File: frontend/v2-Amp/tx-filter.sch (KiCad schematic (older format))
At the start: 98 parts, among them K10 HK4100, K11 HK4100, K12 HK4100, K13 HK4100, K14 HK4100, K15 HK4100, K2 HK4100, K3 HK4100, K4 HK4100, K5 HK4100, K6 HK4100, K7 HK4100, K8 HK4100, K9 HK4100

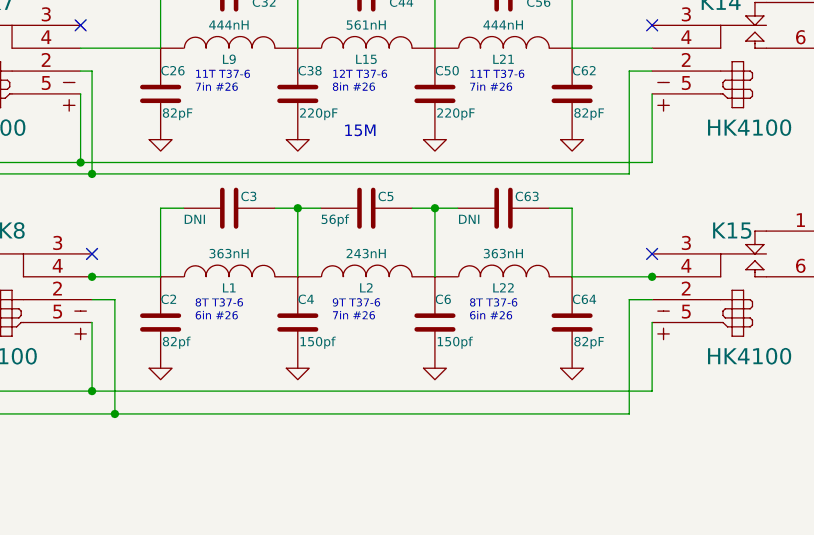
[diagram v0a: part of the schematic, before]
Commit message: Updates to 10M filter
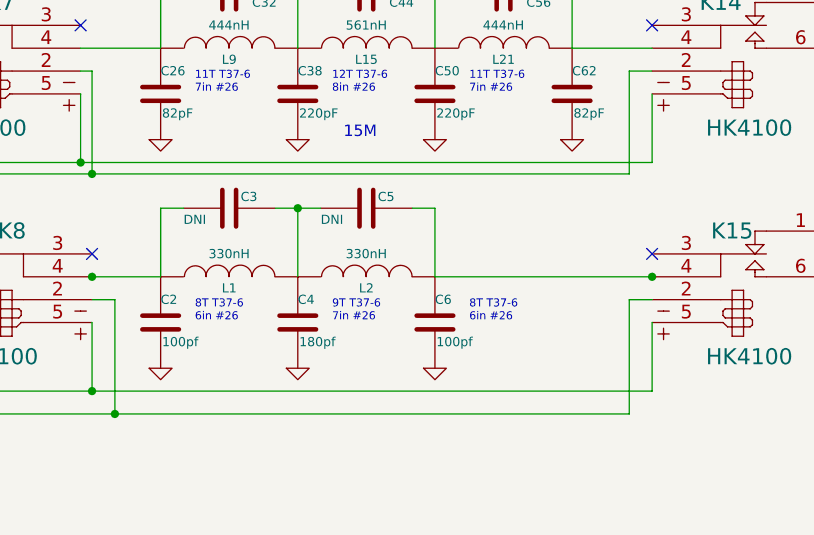
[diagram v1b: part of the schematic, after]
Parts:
- removed C63: DNI, HERMESLITE:C_0805, symbol C-RESCUE-amp
- removed C64: 82pF, HERMESLITE:C_0805, symbol C-RESCUE-amp
- removed L22: 363nH, Resistors_SMD:R_0805_HandSoldering, symbol INDUCTOR
- C2: value 82pf -> 100pf
- C4: value 150pf -> 180pf
- C5: value 56pf -> DNI
- C6: value 150pf -> 100pf
- L1: value 363nH -> 330nH; footprint Resistors_SMD:R_0805_HandSoldering -> HERMESLITE:inductor
- L2: value 243nH -> 330nH; footprint Resistors_SMD:R_0805_HandSoldering -> HERMESLITE:inductor
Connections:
- net at K15.4: now also C5.1, C6.1, L2.2
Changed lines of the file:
@@
 P 3900 6300
 F 0 "L1" V 3850 6300 40  0000 C CNN
-F 1 "363nH" V 4000 6300 40  0000 C CNN
-F 2 "Resistors_SMD:R_0805_HandSoldering" H 3900 6300 60  0001 C CNN
+F 1 "330nH" V 4000 6300 40  0000 C CNN
+F 2 "HERMESLITE:inductor" H 3900 6300 60  0001 C CNN
 F 3 "" H 3900 6300 60  0000 C CNN
 	1    3900 6300
@@
 P 4500 6300
 F 0 "L2" V 4450 6300 40  0000 C CNN
-F 1 "243nH" V 4600 6300 40  0000 C CNN
-F 2 "Resistors_SMD:R_0805_HandSoldering" H 4500 6300 60  0001 C CNN
+F 1 "330nH" V 4600 6300 40  0000 C CNN
+F 2 "HERMESLITE:inductor" H 4500 6300 60  0001 C CNN
 F 3 "" H 4500 6300 60  0000 C CNN
 	1    4500 6300
@@
 P 3600 6500
 F 0 "C2" H 3600 6600 40  0000 L CNN
-F 1 "82pf" H 3606 6415 40  0000 L CNN
+F 1 "100pf" H 3606 6415 40  0000 L CNN
 F 2 "HERMESLITE:C_0805" H 3638 6350 30  0001 C CNN
 F 3 "" H 3600 6500 60  0000 C CNN
@@
 P 4200 6500
 F 0 "C4" H 4200 6600 40  0000 L CNN
-F 1 "150pf" H 4206 6415 40  0000 L CNN
+F 1 "180pf" H 4206 6415 40  0000 L CNN
 F 2 "HERMESLITE:C_0805" H 4238 6350 30  0001 C CNN
 F 3 "" H 4200 6500 60  0000 C CNN
@@
 P 4800 6500
 F 0 "C6" H 4800 6600 40  0000 L CNN
-F 1 "150pf" H 4806 6415 40  0000 L CNN
+F 1 "100pf" H 4806 6415 40  0000 L CNN
 F 2 "HERMESLITE:C_0805" H 4838 6350 30  0001 C CNN
 F 3 "" H 4800 6500 60  0000 C CNN
@@
 P 4500 6000
 F 0 "C5" V 4450 6050 40  0000 L CNN
-F 1 "56pf" V 4550 5800 40  0000 L CNN
+F 1 "DNI" V 4550 5800 40  0000 L CNN
 F 2 "HERMESLITE:C_0805" H 4538 5850 30  0001 C CNN
 F 3 "" H 4500 6000 60  0000 C CNN
@@
 	3600 6000 3700 6000
 Wire Wire Line
-	4700 6000 4900 6000
-Wire Wire Line
 	4800 6000 4800 6300
 Wire Wire Line
@@
 Text Notes 3750 6500 0    35   ~ 0
 8T T37-6\n6in #26
-$Comp
-L INDUCTOR L22
-U 1 1 572770BA
-P 5100 6300
-F 0 "L22" V 5050 6300 40  0000 C CNN
-F 1 "363nH" V 5200 6300 40  0000 C CNN
-F 2 "Resistors_SMD:R_0805_HandSoldering" H 5100 6300 60  0001 C CNN
-F 3 "" H 5100 6300 60  0000 C CNN
-	1    5100 6300
-	0    -1   -1   0
-$EndComp
-$Comp
-L C-RESCUE-amp C64
-U 1 1 572770C1
-P 5400 6500
-F 0 "C64" H 5400 6600 40  0000 L CNN
-F 1 "82pF" H 5406 6415 40  0000 L CNN
-F 2 "HERMESLITE:C_0805" H 5438 6350 30  0001 C CNN
-F 3 "" H 5400 6500 60  0000 C CNN
-	1    5400 6500
-	1    0    0    -1
-$EndComp
-$Comp
-L C-RESCUE-amp C63
-U 1 1 572770C8
-P 5100 6000
-F 0 "C63" V 5050 6050 40  0000 L CNN
-F 1 "DNI" V 5150 5800 40  0000 L CNN
-F 2 "HERMESLITE:C_0805" H 5138 5850 30  0001 C CNN
-F 3 "" H 5100 6000 60  0000 C CNN
-	1    5100 6000
-	0    1    1    0
-$EndComp
 Wire Wire Line
 	4100 6000 4300 6000
-Connection ~ 4800 6000
-Wire Wire Line
-	5300 6000 5400 6000
-Wire Wire Line
-	5400 6000 5400 6300
-$Comp
-L GND-RESCUE-amp #PWR080
-U 1 1 572770D3
-P 5400 6700
-F 0 "#PWR080" H 5400 6700 30  0001 C CNN
-F 1 "GND" H 5400 6630 30  0001 C CNN
-F 2 "" H 5400 6700 60  0000 C CNN
-F 3 "" H 5400 6700 60  0000 C CNN
-	1    5400 6700
-	1    0    0    -1
-$EndComp
 Text Notes 4950 6500 0    35   ~ 0
 8T T37-6\n6in #26
 Wire Wire Line
-	5400 6300 5750 6300
+	4800 6300 5750 6300
 Wire Wire Line
 	3300 6300 3600 6300
+Wire Wire Line
+	4700 6000 4800 6000
 $EndSCHEMATC

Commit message: Updates for v1.1
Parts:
- added C63: DNI, HERMESLITE:C_0805, symbol C-RESCUE-amp
- added C64: 100pf, HERMESLITE:C_0805, symbol C-RESCUE-amp
- added L22: 330nH, HERMESLITE:inductor, symbol INDUCTOR
- C6: value 100pf -> 180pf
- L2: value 330nH -> 270nH
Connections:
- net GND: now also C64.2
- net at C5.1, C6.1, L2.2: now also C63.2, L22.1; no longer K15.4
- new net: C63.1, C64.1, K15.4, L22.2
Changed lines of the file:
@@
 P 4500 6300
 F 0 "L2" V 4450 6300 40  0000 C CNN
-F 1 "330nH" V 4600 6300 40  0000 C CNN
+F 1 "270nH" V 4600 6300 40  0000 C CNN
 F 2 "HERMESLITE:inductor" H 4500 6300 60  0001 C CNN
 F 3 "" H 4500 6300 60  0000 C CNN
@@
 P 4800 6500
 F 0 "C6" H 4800 6600 40  0000 L CNN
-F 1 "100pf" H 4806 6415 40  0000 L CNN
+F 1 "180pf" H 4806 6415 40  0000 L CNN
 F 2 "HERMESLITE:C_0805" H 4838 6350 30  0001 C CNN
 F 3 "" H 4800 6500 60  0000 C CNN
@@
 8T T37-6\n6in #26
 Wire Wire Line
-	4800 6300 5750 6300
-Wire Wire Line
 	3300 6300 3600 6300
 Wire Wire Line
-	4700 6000 4800 6000
+	4700 6000 4900 6000
+$Comp
+L C-RESCUE-amp C63
+U 1 1 573085BC
+P 5100 6000
+F 0 "C63" V 5050 6050 40  0000 L CNN
+F 1 "DNI" V 5150 5800 40  0000 L CNN
+F 2 "HERMESLITE:C_0805" H 5138 5850 30  0001 C CNN
+F 3 "" H 5100 6000 60  0000 C CNN
+	1    5100 6000
+	0    1    1    0
+$EndComp
+$Comp
+L INDUCTOR L22
+U 1 1 57308772
+P 5100 6300
+F 0 "L22" V 5050 6300 40  0000 C CNN
+F 1 "330nH" V 5200 6300 40  0000 C CNN
+F 2 "HERMESLITE:inductor" H 5100 6300 60  0001 C CNN
+F 3 "" H 5100 6300 60  0000 C CNN
+	1    5100 6300
+	0    -1   -1   0
+$EndComp
+$Comp
+L C-RESCUE-amp C64
+U 1 1 573088BB
+P 5400 6500
+F 0 "C64" H 5400 6600 40  0000 L CNN
+F 1 "100pf" H 5406 6415 40  0000 L CNN
+F 2 "HERMESLITE:C_0805" H 5438 6350 30  0001 C CNN
+F 3 "" H 5400 6500 60  0000 C CNN
+	1    5400 6500
+	1    0    0    -1
+$EndComp
+$Comp
+L GND-RESCUE-amp #PWR080
+U 1 1 57308A09
+P 5400 6700
+F 0 "#PWR080" H 5400 6700 30  0001 C CNN
+F 1 "GND" H 5400 6630 30  0001 C CNN
+F 2 "" H 5400 6700 60  0000 C CNN
+F 3 "" H 5400 6700 60  0000 C CNN
+	1    5400 6700
+	1    0    0    -1
+$EndComp
+Wire Wire Line
+	5400 6300 5750 6300
+Wire Wire Line
+	5300 6000 5400 6000
+Wire Wire Line
+	5400 6000 5400 6300
+Connection ~ 4800 6000
 $EndSCHEMATC
